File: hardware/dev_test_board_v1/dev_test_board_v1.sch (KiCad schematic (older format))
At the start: 39 parts

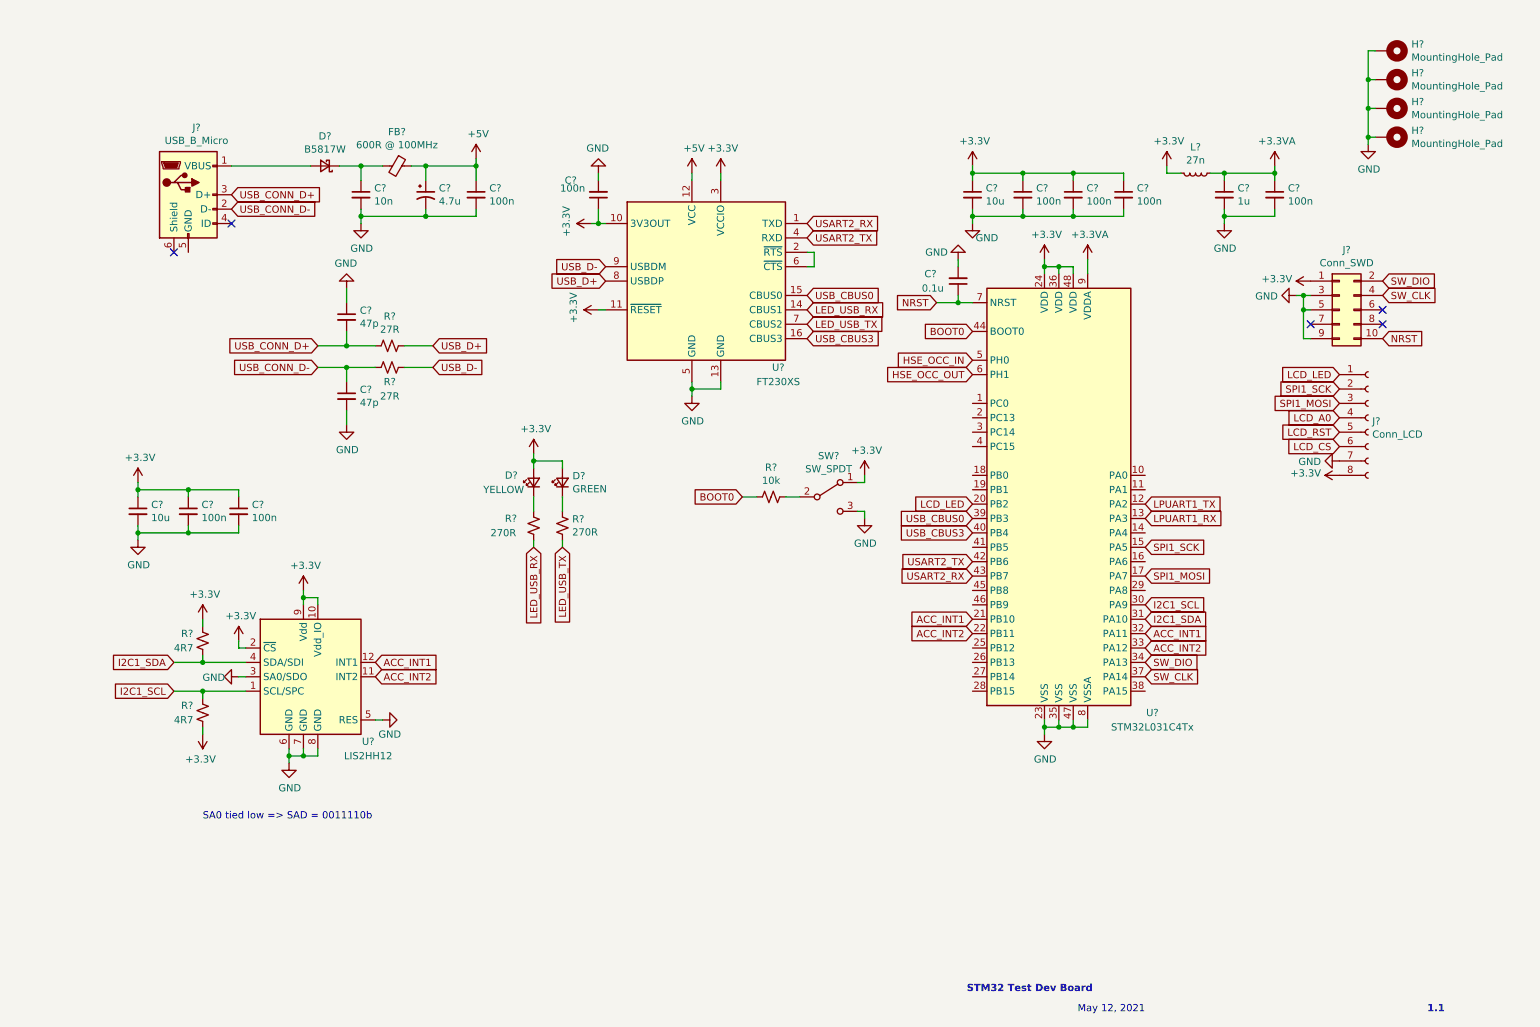
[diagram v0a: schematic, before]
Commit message: All needed pins assigned.
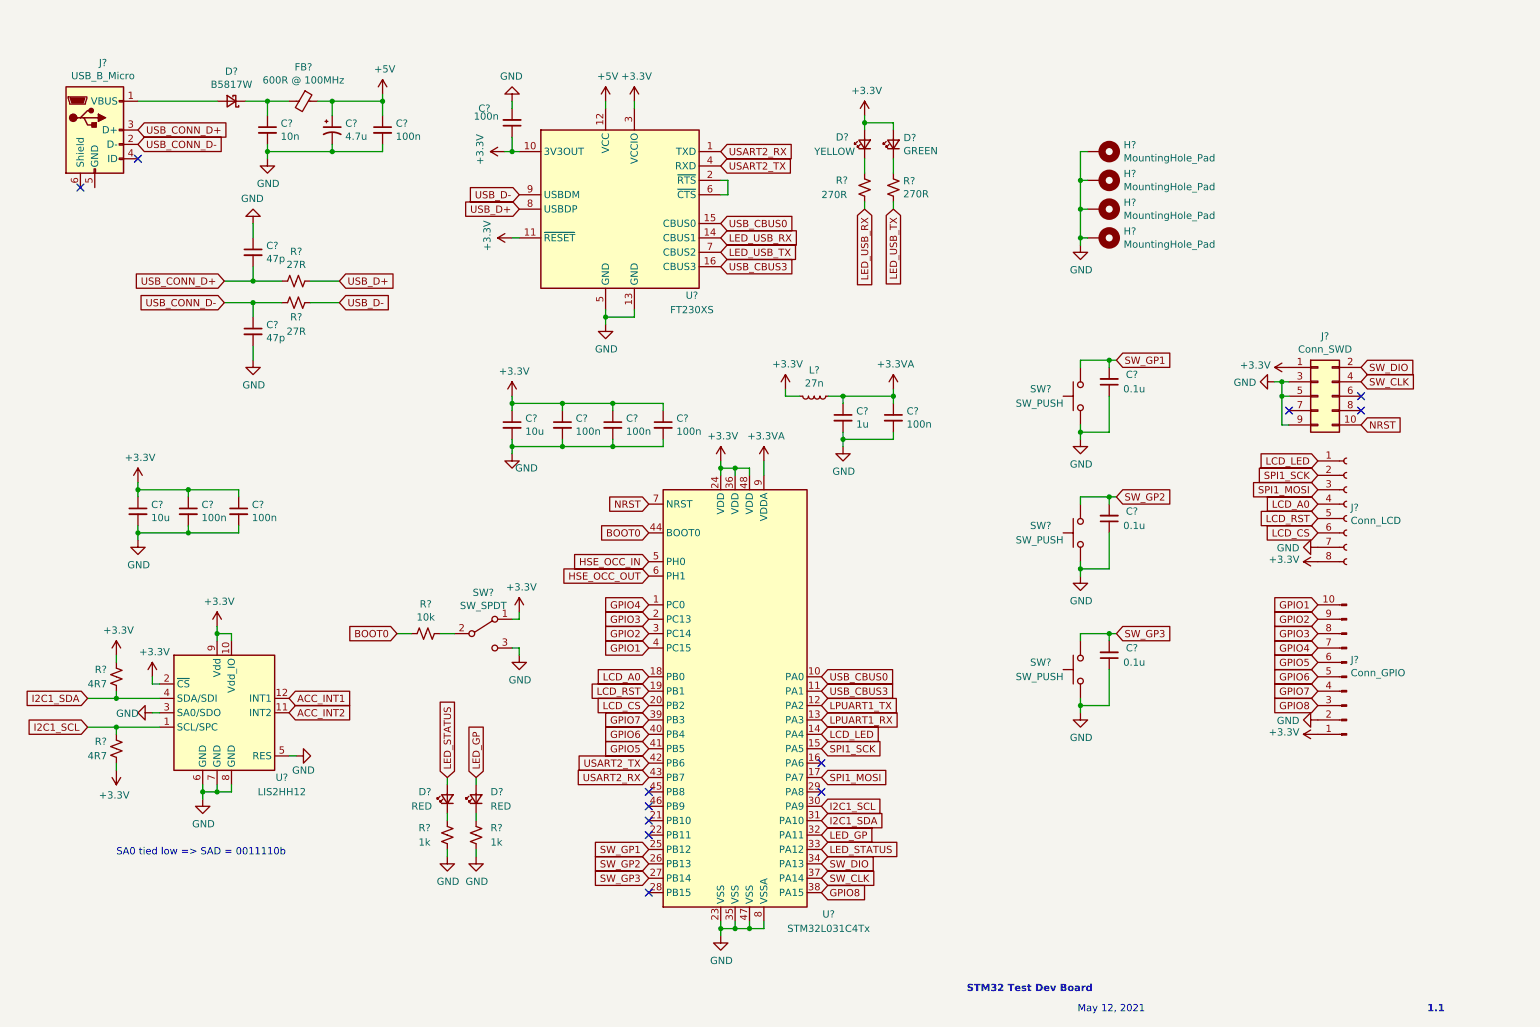
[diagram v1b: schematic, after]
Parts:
- added C? (x2): 0.1u, symbol Device:C_Small
- added D? (x2): RED, symbol Device:LED_Small
- added J?: Conn_GPIO, symbol Connector:Conn_01x10_Male
- added R? (x2): 1k, symbol Device:R_Small_US
- added SW? (x3): SW_PUSH, symbol Switch:SW_Push
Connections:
- net +3V3: now also J?.1 (Pin_1)
- net ACC_INT1: no longer U?.21 (PB10), U?.32 (PA11)
- net ACC_INT2: no longer U?.22 (PB11), U?.33 (PA12)
- net GND: now also C?.1, C?.1, C?.1, J?.2 (Pin_2), R?.2, R?.2, SW?.1, SW?.1, SW?.1; no longer C?.2
- net LCD_A0: now also U?.18 (PB0)
- net LCD_CS: now also U?.20 (PB2)
- net LCD_LED: now also U?.14 (PA4); no longer U?.20 (PB2)
- net LCD_RST: now also U?.19 (PB1)
- net NRST: no longer C?.1
- net USB_CBUS0: now also U?.10 (PA0); no longer U?.39 (PB3)
- net USB_CBUS3: now also U?.11 (PA1); no longer U?.40 (PB4)
- net GPIO4: now reaches U?.1 (PC0)
- net GPIO4: now also J?.7 (Pin_7)
- net GPIO3: now reaches U?.2 (PC13)
- net GPIO3: now also J?.8 (Pin_8)
- net SW_GP1: now reaches U?.25 (PB12)
- net SW_GP1: now also C?.2, SW?.2
- net SW_GP2: now reaches U?.26 (PB13)
- net SW_GP2: now also C?.2, SW?.2
- net SW_GP3: now reaches U?.27 (PB14)
- net SW_GP3: now also C?.2, SW?.2
- net GPIO2: now reaches U?.3 (PC14)
- net GPIO2: now also J?.9 (Pin_9)
- net GPIO8: now reaches U?.38 (PA15)
- net GPIO8: now also J?.3 (Pin_3)
- net GPIO1: now reaches U?.4 (PC15)
- net GPIO1: now also J?.10 (Pin_10)
- net GPIO5: now reaches U?.41 (PB5)
- net GPIO5: now also J?.6 (Pin_6)
- new net: D?.1 (K), R?.1 (x2)
- new net GPIO6: J?.5 (Pin_5), U?.40 (PB4)
- new net GPIO7: J?.4 (Pin_4), U?.39 (PB3)
- new net LED_GP: D?.2 (A), U?.32 (PA11)
- new net LED_STATUS: D?.2 (A), U?.33 (PA12)
- no-connect marks 5 -> 12
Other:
- moved on the sheet: C?, D?, FB?, H?, J?, L?, R?, SW?, U?

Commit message: Components labelled, HSE oscillator added.
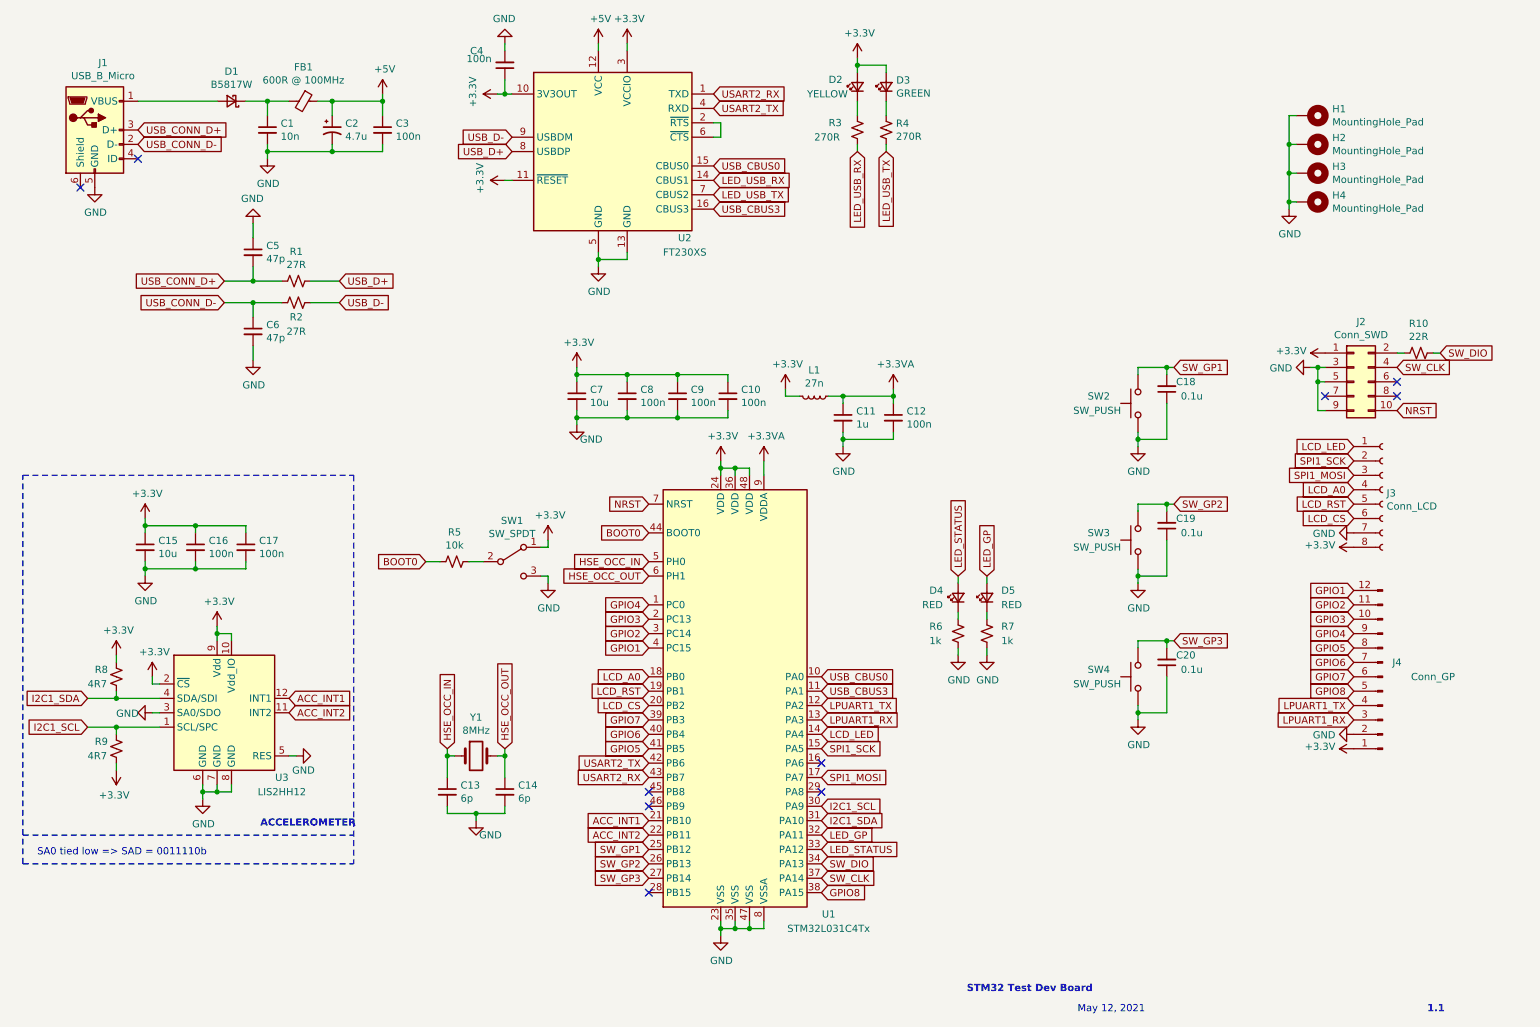
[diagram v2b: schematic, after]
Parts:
- removed J?: Conn_GPIO, symbol Connector:Conn_01x10_Male
- added C13, C14: 6p, symbol Device:C_Small
- added J4: Conn_GP, symbol Connector:Conn_01x12_Male
- added R10: 22R, symbol Device:R_Small_US
- added Y1: 8MHz, symbol Device:Crystal
- gave numbers to parts that had none: 48
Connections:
- net +3V3: now also J4.1 (Pin_1)
- net ACC_INT1: now also U1.21 (PB10)
- net ACC_INT2: now also U1.22 (PB11)
- net GND: now also J1.5 (GND), C13.2, C14.2, J4.2 (Pin_2)
- net GPIO1: now also J4.12 (Pin_12)
- net GPIO2: now also J4.11 (Pin_11)
- net GPIO3: now also J4.10 (Pin_10)
- net GPIO4: now also J4.9 (Pin_9)
- net GPIO5: now also J4.8 (Pin_8)
- net GPIO6: now also J4.7 (Pin_7)
- net GPIO7: now also J4.6 (Pin_6)
- net GPIO8: now also J4.5 (Pin_5)
- net HSE_OCC_IN: now also C13.1, Y1.1
- net HSE_OCC_OUT: now also C14.1, Y1.2
- net LPUART1_RX: now also J4.3 (Pin_3)
- net LPUART1_TX: now also J4.4 (Pin_4)
- net SW_DIO: now also R10.1; no longer J2.2 (Pin_2)
- new net: J2.2 (Pin_2), R10.2
- no-connect marks 12 -> 10
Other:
- note added: "ACCELEROMETER\n"
- moved on the sheet: C10, C15, C16, C17, C18, C19, C20, C4, C7, C8, C9, D2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

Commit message: Started PCB layout.
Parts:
- removed D1: B5817W, symbol Device:D_Schottky_Small
- C1, C18, C19, C20, C5, C6: footprint (none) -> Capacitor_SMD:C_0603_1608Metric
- C10, C11, C12, C13, C14, C15, C16, C17, C3, C4, C7, C8, C9: footprint (none) -> Capacitor_SMD:C_0402_1005Metric
- C2: footprint (none) -> Capacitor_SMD:CP_Elec_4x5.4
- D2, D3, D4: footprint (none) -> LED_SMD:LED_0603_1608Metric
- D5: value RED -> BLUE; footprint (none) -> LED_SMD:LED_0603_1608Metric
- FB1: footprint (none) -> Inductor_SMD:L_0805_2012Metric
- H1, H2, H3, H4: footprint (none) -> MountingHole:MountingHole_2.7mm_M2.5_Pad_Via
- J1: footprint (none) -> Connector_USB:USB_Micro-B_GCT_USB3076-30-A
- J2: footprint (none) -> Connector_PinHeader_1.27mm:PinHeader_2x05_P1.27mm_Vertical
- J3: footprint (none) -> Connector_PinSocket_2.54mm:PinSocket_1x08_P2.54mm_Vertical
- J4: footprint (none) -> Connector_PinHeader_2.54mm:PinHeader_1x12_P2.54mm_Vertical
- L1: footprint (none) -> Inductor_SMD:L_0603_1608Metric
- R1, R10, R2, R5, R8, R9: footprint (none) -> Resistor_SMD:R_0402_1005Metric
- R3, R4, R6, R7: footprint (none) -> Resistor_SMD:R_0603_1608Metric
- SW1: footprint (none) -> Button_Switch_SMD:SW_SPDT_PCM12
- SW2, SW3, SW4: footprint (none) -> Button_Switch_SMD:SW_Push_1P1T_NO_6x6mm_H9.5mm
- Y1: footprint (none) -> tyjba_footprints:Crystal_NX8045GB
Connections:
- net at J1.1 (VBUS): now also C1.1, FB1.2
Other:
- note added: "Must be configured in SW."
- note added: "Pull-up resistors internal.\n"
- moved on the sheet: C1, C2, C3, FB1

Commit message: Draft layout complete.
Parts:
- SW1: footprint Button_Switch_SMD:SW_SPDT_PCM12 -> tyjba_footprints:SW_Unknown_SPDT_Straight
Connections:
- net +3V3: now also J3.1 (Pin_1); no longer J3.8 (Pin_8)
- net GND: now also J3.2 (Pin_2); no longer J3.7 (Pin_7)
- net LCD_A0: now also J3.5 (Pin_5), U1.19 (PB1); no longer J3.4 (Pin_4), U1.18 (PB0)
- net LCD_CS: now also J3.3 (Pin_3), U1.14 (PA4); no longer J3.6 (Pin_6), U1.20 (PB2)
- net LCD_LED: now also J3.8 (Pin_8), U1.20 (PB2); no longer J3.1 (Pin_1), U1.14 (PA4)
- net LCD_RST: now also J3.4 (Pin_4), U1.18 (PB0); no longer J3.5 (Pin_5), U1.19 (PB1)
- net SPI1_MOSI: now also J3.6 (Pin_6); no longer J3.3 (Pin_3)
- net SPI1_SCK: now also J3.7 (Pin_7); no longer J3.2 (Pin_2)
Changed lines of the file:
@@
 L power:GND #PWR0125
 U 1 1 609DBE90
-P 10050 4300
-F 0 "#PWR0125" H 10050 4050 50  0001 C CNN
-F 1 "GND" V 10055 4172 50  0000 R CNN
-F 2 "" H 10050 4300 50  0001 C CNN
-F 3 "" H 10050 4300 50  0001 C CNN
-	1    10050 4300
+P 10050 3800
+F 0 "#PWR0125" H 10050 3550 50  0001 C CNN
+F 1 "GND" V 10055 3672 50  0000 R CNN
+F 2 "" H 10050 3800 50  0001 C CNN
+F 3 "" H 10050 3800 50  0001 C CNN
+	1    10050 3800
 	0    1    1    0
 $EndComp
@@
 L power:+3.3V #PWR0124
 U 1 1 609DA543
-P 10050 4400
-F 0 "#PWR0124" H 10050 4250 50  0001 C CNN
-F 1 "+3.3V" V 10065 4528 50  0000 L CNN
-F 2 "" H 10050 4400 50  0001 C CNN
-F 3 "" H 10050 4400 50  0001 C CNN
-	1    10050 4400
+P 10050 3700
+F 0 "#PWR0124" H 10050 3550 50  0001 C CNN
+F 1 "+3.3V" V 10065 3828 50  0000 L CNN
+F 2 "" H 10050 3700 50  0001 C CNN
+F 3 "" H 10050 3700 50  0001 C CNN
+	1    10050 3700
 	0    -1   -1   0
 $EndComp
+Text GLabel 10050 4200 0    50   Input ~ 0
+SPI1_MOSI
+Text GLabel 10050 4300 0    50   Input ~ 0
+SPI1_SCK
 Text GLabel 10050 3900 0    50   Input ~ 0
-SPI1_MOSI
-Text GLabel 10050 3800 0    50   Input ~ 0
-SPI1_SCK
-Text GLabel 10050 4200 0    50   Input ~ 0
 LCD_CS
+Text GLabel 10050 4000 0    50   Input ~ 0
+LCD_RST
 Text GLabel 10050 4100 0    50   Input ~ 0
-LCD_RST
-Text GLabel 10050 4000 0    50   Input ~ 0
 LCD_A0
-Text GLabel 10050 3700 0    50   Input ~ 0
+Text GLabel 10050 4400 0    50   Input ~ 0
 LCD_LED
 $Comp
@@
 Text GLabel 6350 6500 2    50   Input ~ 0
 LED_STATUS
+Text GLabel 6350 5700 2    50   Input ~ 0
+LCD_CS
+Text GLabel 5150 5300 0    50   Input ~ 0
+LCD_RST
+Text GLabel 5150 5400 0    50   Input ~ 0
+LCD_A0
 Text GLabel 5150 5500 0    50   Input ~ 0
-LCD_CS
-Text GLabel 5150 5400 0    50   Input ~ 0
-LCD_RST
-Text GLabel 5150 5300 0    50   Input ~ 0
-LCD_A0
-Text GLabel 6350 5700 2    50   Input ~ 0
 LCD_LED
 Text GLabel 6350 5400 2    50   Input ~ 0
@@
 F 0 "SW1" H 4200 4785 50  0000 C CNN
 F 1 "SW_SPDT" H 4200 4694 50  0000 C CNN
-F 2 "Button_Switch_SMD:SW_SPDT_PCM12" H 4200 4500 50  0001 C CNN
+F 2 "tyjba_footprints:SW_Unknown_SPDT_Straight" H 4200 4500 50  0001 C CNN
 F 3 "~" H 4200 4500 50  0001 C CNN
 	1    4200 4500

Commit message: All signals routed.
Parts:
- J1: footprint Connector_USB:USB_Micro-B_GCT_USB3076-30-A -> tyjba_footprints:UBS_Micro-B_Citzends_Aliexpress
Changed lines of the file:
@@
 F 0 "J1" H 1357 1967 50  0000 C CNN
 F 1 "USB_B_Micro" H 1357 1876 50  0000 C CNN
-F 2 "Connector_USB:USB_Micro-B_GCT_USB3076-30-A" H 1450 1450 50  0001 C CNN
+F 2 "tyjba_footprints:UBS_Micro-B_Citzends_Aliexpress" H 1450 1450 50  0001 C CNN
 F 3 "~" H 1450 1450 50  0001 C CNN
 	1    1300 1500
